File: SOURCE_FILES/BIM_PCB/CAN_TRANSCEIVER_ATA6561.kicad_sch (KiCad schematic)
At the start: 5 parts, among them U9 ATA6561-GAQW-N

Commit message: updates on schematic and complete layout
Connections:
- net CANH renamed B_to_CANH
- net CANL renamed A_to_CANL
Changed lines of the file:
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@@
   (junction (at 62.23 88.9) (diameter 0) (color 0 0 0 0)
-  )
-  (junction (at 162.56 88.9) (diameter 0) (color 0 0 0 0)
   )
   (junction (at 167.64 105.41) (diameter 0) (color 0 0 0 0)
   )
-  (junction (at 172.72 83.82) (diameter 0) (color 0 0 0 0)
+  (junction (at 152.4 83.82) (diameter 0) (color 0 0 0 0)
   )
-  (wire (pts (xy 171.45 87.63) (xy 173.99 87.63))
-    (stroke (width 0) (type default))
+  (junction (at 152.4 88.9) (diameter 0) (color 0 0 0 0)
   )
   (wire (pts (xy 54.61 90.17) (xy 54.61 88.9))
@@
     (stroke (width 0) (type default))
   )
-  (wire (pts (xy 172.72 93.98) (xy 172.72 83.82))
+  (wire (pts (xy 152.4 88.9) (xy 162.56 88.9))
     (stroke (width 0) (type default))
   )
-  (wire (pts (xy 208.28 85.09) (xy 201.93 85.09))
+  (wire (pts (xy 172.72 93.98) (xy 172.72 83.82))
     (stroke (width 0) (type default))
   )
@@
     (stroke (width 0) (type default))
   )
-  (wire (pts (xy 201.93 85.09) (xy 201.93 83.82))
+  (wire (pts (xy 139.7 62.23) (xy 139.7 67.31))
     (stroke (width 0) (type default))
   )
-  (wire (pts (xy 139.7 62.23) (xy 139.7 67.31))
+  (wire (pts (xy 152.4 88.9) (xy 152.4 91.44))
     (stroke (width 0) (type default))
   )
@@
     (stroke (width 0) (type default))
   )
-  (wire (pts (xy 201.93 87.63) (xy 201.93 88.9))
+  (wire (pts (xy 129.54 83.82) (xy 152.4 83.82))
     (stroke (width 0) (type default))
   )
-  (wire (pts (xy 173.99 88.9) (xy 201.93 88.9))
+  (wire (pts (xy 152.4 83.82) (xy 172.72 83.82))
     (stroke (width 0) (type default))
   )
-  (wire (pts (xy 173.99 87.63) (xy 173.99 88.9))
-    (stroke (width 0) (type default))
-  )
-  (wire (pts (xy 129.54 83.82) (xy 172.72 83.82))
+  (wire (pts (xy 152.4 78.74) (xy 152.4 83.82))
     (stroke (width 0) (type default))
   )
   (wire (pts (xy 74.93 83.82) (xy 104.14 83.82))
-    (stroke (width 0) (type default))
-  )
-  (wire (pts (xy 171.45 88.9) (xy 171.45 87.63))
-    (stroke (width 0) (type default))
-  )
-  (wire (pts (xy 208.28 87.63) (xy 201.93 87.63))
-    (stroke (width 0) (type default))
-  )
-  (wire (pts (xy 172.72 83.82) (xy 201.93 83.82))
-    (stroke (width 0) (type default))
-  )
-  (wire (pts (xy 162.56 88.9) (xy 171.45 88.9))
     (stroke (width 0) (type default))
   )
@@
     (stroke (width 0) (type default))
   )
-  (wire (pts (xy 129.54 88.9) (xy 162.56 88.9))
+  (wire (pts (xy 129.54 88.9) (xy 152.4 88.9))
     (stroke (width 0) (type default))
   )
@@
     (effects (font (face "Agency FB") (size 5 5) (thickness 0.4) bold) (justify left bottom))
   )
+  (global_label "B_to_CANH" (shape input) (at 152.4 78.74 90) (fields_autoplaced)
+    (effects (font (size 1.27 1.27)) (justify left))
+    (property "Intersheetrefs" "${INTERSHEET_REFS}" (at 152.4 65.7347 90)
+      (effects (font (size 1.27 1.27)) (justify left) hide)
+    )
+  )
+  (global_label "A_to_CANL" (shape input) (at 152.4 91.44 270) (fields_autoplaced)
+    (effects (font (size 1.27 1.27)) (justify right))
+    (property "Intersheetrefs" "${INTERSHEET_REFS}" (at 152.4 103.9615 90)
+      (effects (font (size 1.27 1.27)) (justify right) hide)
+    )
+  )
   (hierarchical_label "CAN_RX" (shape input) (at 74.93 83.82 180) (fields_autoplaced)
     (effects (font (size 1.27 1.27) bold) (justify right))
-  )
-  (hierarchical_label "CANH" (shape input) (at 208.28 85.09 0) (fields_autoplaced)
-    (effects (font (size 1.27 1.27) bold) (justify left))
   )
   (hierarchical_label "CAN_STBY" (shape input) (at 74.93 91.44 180) (fields_autoplaced)
     (effects (font (size 1.27 1.27) bold) (justify right))
   )
-  (hierarchical_label "CANL" (shape input) (at 208.28 87.63 0) (fields_autoplaced)
-    (effects (font (size 1.27 1.27) bold) (justify left))
-  )
   (hierarchical_label "CAN_TX" (shape output) (at 74.93 81.28 180) (fields_autoplaced)

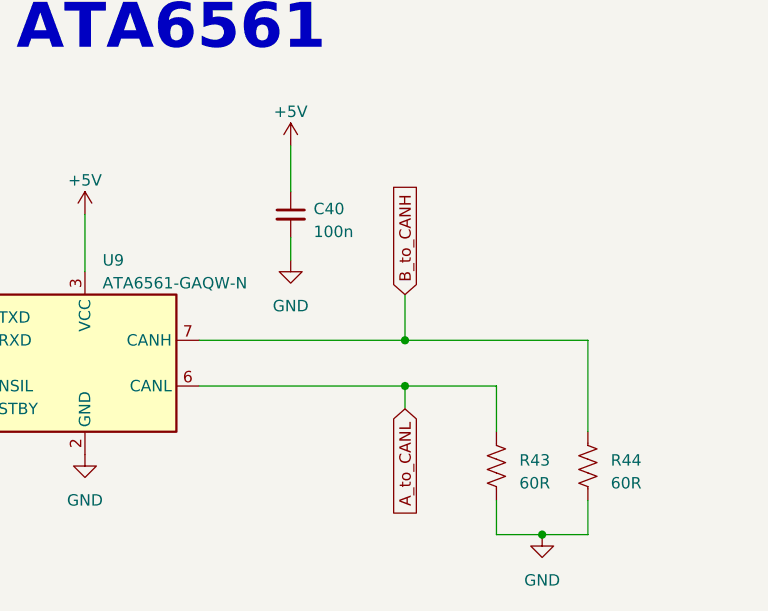
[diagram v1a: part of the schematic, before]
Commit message: completed design PCN and Images
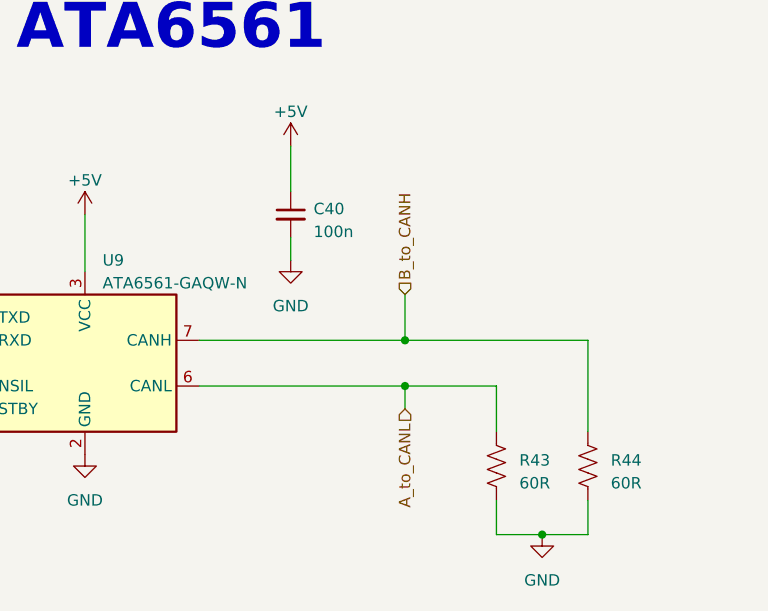
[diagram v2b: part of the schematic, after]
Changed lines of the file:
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@@
     (effects (font (face "Agency FB") (size 5 5) (thickness 0.4) bold) (justify left bottom))
-  )
-  (global_label "B_to_CANH" (shape input) (at 152.4 78.74 90) (fields_autoplaced)
-    (effects (font (size 1.27 1.27)) (justify left))
-    (property "Intersheetrefs" "${INTERSHEET_REFS}" (at 152.4 65.7347 90)
-      (effects (font (size 1.27 1.27)) (justify left) hide)
-    )
-  )
-  (global_label "A_to_CANL" (shape input) (at 152.4 91.44 270) (fields_autoplaced)
-    (effects (font (size 1.27 1.27)) (justify right))
-    (property "Intersheetrefs" "${INTERSHEET_REFS}" (at 152.4 103.9615 90)
-      (effects (font (size 1.27 1.27)) (justify right) hide)
-    )
   )
   (hierarchical_label "CAN_RX" (shape input) (at 74.93 83.82 180) (fields_autoplaced)
     (effects (font (size 1.27 1.27) bold) (justify right))
   )
+  (hierarchical_label "A_to_CANL" (shape input) (at 152.4 91.44 270) (fields_autoplaced)
+    (effects (font (size 1.27 1.27)) (justify right))
+  )
   (hierarchical_label "CAN_STBY" (shape input) (at 74.93 91.44 180) (fields_autoplaced)
     (effects (font (size 1.27 1.27) bold) (justify right))
   )
+  (hierarchical_label "B_to_CANH" (shape input) (at 152.4 78.74 90) (fields_autoplaced)
+    (effects (font (size 1.27 1.27)) (justify left))
+  )
   (hierarchical_label "CAN_TX" (shape output) (at 74.93 81.28 180) (fields_autoplaced)
     (effects (font (size 1.27 1.27) bold) (justify right))
@@
           (reference "C41") (unit 1)
         )
+        (path "/b79ebed7-e146-448b-8dab-0aefb3e182ca/8f0f6c30-1fa5-47af-a908-64d0452989fe"
+          (reference "C44") (unit 1)
+        )
       )
     )
@@
           (reference "C40") (unit 1)
         )
+        (path "/b79ebed7-e146-448b-8dab-0aefb3e182ca/8f0f6c30-1fa5-47af-a908-64d0452989fe"
+          (reference "C43") (unit 1)
+        )
       )
     )
@@
           (reference "R43") (unit 1)
         )
+        (path "/b79ebed7-e146-448b-8dab-0aefb3e182ca/8f0f6c30-1fa5-47af-a908-64d0452989fe"
+          (reference "R59") (unit 1)
+        )
       )
     )
@@
           (reference "#PWR076") (unit 1)
         )
+        (path "/b79ebed7-e146-448b-8dab-0aefb3e182ca/8f0f6c30-1fa5-47af-a908-64d0452989fe"
+          (reference "#PWR090") (unit 1)
+        )
       )
     )
@@
           (reference "#PWR079") (unit 1)
         )
+        (path "/b79ebed7-e146-448b-8dab-0aefb3e182ca/8f0f6c30-1fa5-47af-a908-64d0452989fe"
+          (reference "#PWR093") (unit 1)
+        )
       )
     )
@@
           (reference "#PWR075") (unit 1)
         )
+        (path "/b79ebed7-e146-448b-8dab-0aefb3e182ca/8f0f6c30-1fa5-47af-a908-64d0452989fe"
+          (reference "#PWR089") (unit 1)
+        )
       )
     )
@@
           (reference "#PWR081") (unit 1)
         )
+        (path "/b79ebed7-e146-448b-8dab-0aefb3e182ca/8f0f6c30-1fa5-47af-a908-64d0452989fe"
+          (reference "#PWR095") (unit 1)
+        )
       )
     )
@@
           (reference "#PWR078") (unit 1)
         )
+        (path "/b79ebed7-e146-448b-8dab-0aefb3e182ca/8f0f6c30-1fa5-47af-a908-64d0452989fe"
+          (reference "#PWR092") (unit 1)
+        )
       )
     )
@@
         (path "/b79ebed7-e146-448b-8dab-0aefb3e182ca/9aa00ea0-8ab5-4ecf-8a0c-229fcfe4faab"
           (reference "#PWR080") (unit 1)
+        )
+        (path "/b79ebed7-e146-448b-8dab-0aefb3e182ca/8f0f6c30-1fa5-47af-a908-64d0452989fe"
+          (reference "#PWR094") (unit 1)
         )
       )
@@
           (reference "U9") (unit 1)
         )
+        (path "/b79ebed7-e146-448b-8dab-0aefb3e182ca/8f0f6c30-1fa5-47af-a908-64d0452989fe"
+          (reference "U13") (unit 1)
+        )
       )
     )
@@
           (reference "#PWR077") (unit 1)
         )
+        (path "/b79ebed7-e146-448b-8dab-0aefb3e182ca/8f0f6c30-1fa5-47af-a908-64d0452989fe"
+          (reference "#PWR091") (unit 1)
+        )
       )
     )
@@
           (reference "R44") (unit 1)
         )
-      )
+        (path "/b79ebed7-e146-448b-8dab-0aefb3e182ca/8f0f6c30-1fa5-47af-a908-64d0452989fe"
+          (reference "R60") (unit 1)
+        )
+      )
